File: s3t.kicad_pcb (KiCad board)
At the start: 2 copper layers, 1 part

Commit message: add some lib
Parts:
- removed REF**: S3Core, s3core:S3Core
- added C1, C5: 10uF, Capacitors_SMD:C_0805, F.Cu at (148.5, 105.0)
- added C10, C14, C17, C19, C9: 0.1uF, Capacitors_SMD:C_0603, F.Cu at (148.5, 105.0)
- added C18: 4.7uF, Capacitors_SMD:C_0603, F.Cu at (148.5, 105.0)
- added C2, C4: 100nF, Capacitors_SMD:C_0603, F.Cu at (148.5, 105.0)
- added C3: C, Resistors_SMD:R_0603, F.Cu at (148.5, 105.0)
- added C6: 47uF, Capacitors_THT:CP_Radial_D8.0mm_P2.50mm, F.Cu at (148.5, 105.0)
- added C7, C8: 7pF, Capacitors_SMD:C_0603, F.Cu at (148.5, 105.0)
- added D1, D2: BAV99LT1G, TO_SOT_Packages_SMD:SOT-23, F.Cu at (148.5, 105.0)
- added D3, D4, D5: LED, LEDs:LED_0805, F.Cu at (148.5, 105.0)
- added D6: D, Diodes_SMD:D_1206, F.Cu at (148.5, 105.0)
- added J3: USB_OTG, Connectors:USB_Mini-B, F.Cu at (148.5, 105.0)
- added L1: 1uH, Inductors_SMD:L_7.3x7.3_H3.5, F.Cu at (148.5, 105.0)
- added L2: 1uH, Inductors_SMD:L_1812, F.Cu at (148.5, 105.0)
- added R1: 100K, Resistors_SMD:R_0603, F.Cu at (148.5, 105.0)
- added R10, R6, R8, R9: R, Resistors_SMD:R_0603, F.Cu at (148.5, 105.0)
- added R12, R14: 1K, Resistors_SMD:R_0603, F.Cu at (148.5, 105.0)
- added R17: 10K, Resistors_SMD:R_0603, F.Cu at (148.5, 105.0)
- added R18: 10K2, Capacitors_SMD:C_0603, F.Cu at (148.5, 105.0)
- added R2: 6.8K, Resistors_SMD:R_0603, F.Cu at (148.5, 105.0)
- added R3, R4: 8.2K, Resistors_SMD:R_0603, F.Cu at (148.5, 105.0)
- added R5, R7: 12K, Resistors_SMD:R_0603, F.Cu at (148.5, 105.0)
- added U1: AMS1117-3.3, TO_SOT_Packages_SMD:SOT-223, F.Cu at (148.5, 105.0)
- added U2: TF_CARD, tfcard:tfcard, F.Cu at (148.5, 105.0)
- added U3: s3core, s3core:S3Core, F.Cu at (148.5, 105.0)
- added U4: SX1308, TO_SOT_Packages_SMD:SOT-23-6, F.Cu at (148.5, 105.0)
- added U5: PT4103, TO_SOT_Packages_SMD:SOT-23-6, F.Cu at (148.5, 105.0)
- added U6: THERMAL, fpc36:Hirose_FH12-36S-0.5SH_1x36-1MP_P0.50mm_Horizontal, F.Cu at (148.5, 105.0)
- added U7: LCD_A050FW01, fpc40:Hirose_FH12-40S-0.5SH_1x40-1MP_P0.50mm_Horizontal, F.Cu at (148.5, 105.0)

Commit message: update pcb lib
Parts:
- added C15: C, Capacitors_SMD:C_0603, F.Cu at (86.0, 79.4)
- added J1: DEBUG_UART0, Connectors_JST:JST_EH_B04B-EH-A_04x2.50mm_Straight, F.Cu at (133.2, 67.6)
- added R15: R, Resistors_SMD:R_0805, F.Cu at (50.5, 61.9)
- added R16: R, Resistors_SMD:R_0805, F.Cu at (67.6, 56.8)
- added SW1: SW_DIP_x01, tfcard:button, F.Cu at (87.3, 100.7)
- added SW2: SW_DIP_x01, tfcard:button, F.Cu at (64.0, 136.7)
- added SW3: SW_DIP_x01, tfcard:button, F.Cu at (91.8, 51.6)
- added SW4: SW_DIP_x01, tfcard:button, F.Cu at (68.3, 65.9)
- added SW5: SW_DIP_x01, tfcard:button, F.Cu at (39.1, 81.2)
- added SW6: SW_DIP_x01, tfcard:button, F.Cu at (70.3, 45.2)
- C3: value C -> 0.1uF
- L1: footprint Inductors_SMD:L_7.3x7.3_H3.5 -> Inductors_SMD:L_1812
- R6: value R -> 10K
- moved L1 116.4 mm to (46.0, 49.8)
- moved U1 58.8 mm to (203.5, 84.3)
- moved U3 46.2 mm to (192.3, 119.6)
- moved U2 36.1 mm to (144.9, 140.9)
- moved C6 25.5 mm to (126.3, 92.4)
- moved C1 25.4 mm to (172.6, 97.0)
- moved U7 23.5 mm to (162.8, 86.4)
- moved U6 19.3 mm to (129.6, 109.1)
- moved C2 17.9 mm to (163.4, 114.8)
- moved L2 16.8 mm to (165.1, 107.6)
- moved J3 14.0 mm to (139.4, 94.4)
- moved D1 13.4 mm to (161.1, 100.4)
- moved C4 11.5 mm to (150.3, 116.4)
- moved D2 9.74 mm to (156.4, 110.6)
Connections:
- U2 pad 12: GND -> (no net)

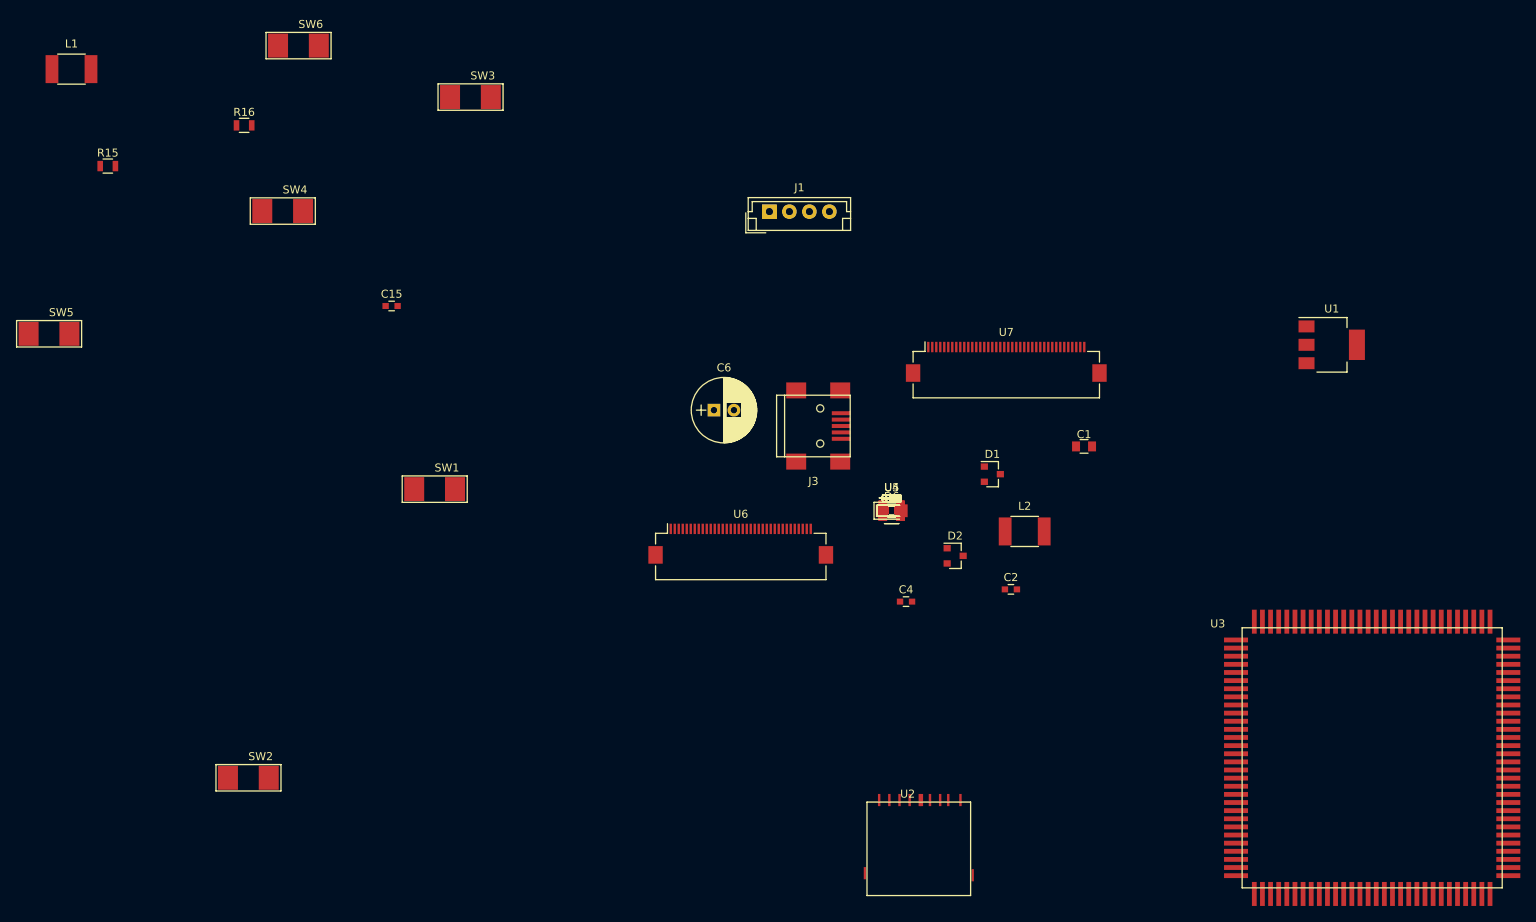
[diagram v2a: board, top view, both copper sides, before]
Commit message: update pcb route
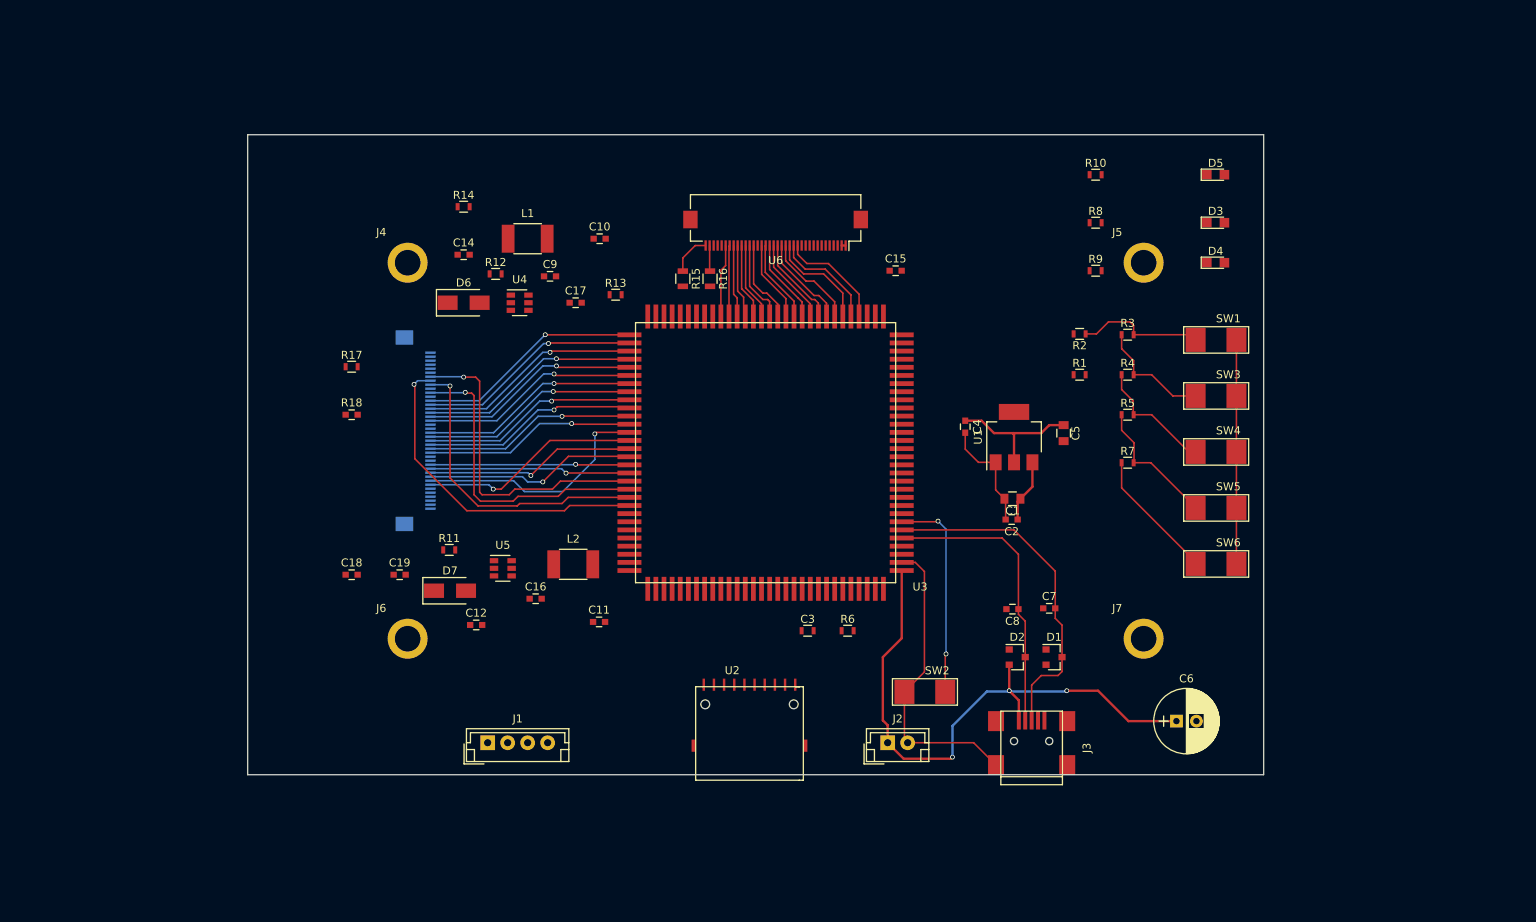
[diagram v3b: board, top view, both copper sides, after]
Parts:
- added C11: 0.1uF, Capacitors_SMD:C_0603, F.Cu at (111.9, 118.9)
- added C12: 0.1uF, Capacitors_SMD:C_0603, F.Cu at (96.6, 119.3)
- added C16: 0.1uF, Capacitors_SMD:C_0603, F.Cu at (104.0, 116.0)
- added D7: D, Diodes_SMD:D_SMA, F.Cu at (93.3, 115.0)
- added J2: Conn_01x02, Connectors_JST:JST_EH_B02B-EH-A_02x2.50mm_Straight, F.Cu at (148.0, 134.0)
- added J4: HOLE, hole:hole, F.Cu at (88.0, 74.0)
- added J5: HOLE, hole:hole, F.Cu at (180.0, 74.0)
- added J6: HOLE, hole:hole, F.Cu at (88.0, 121.0)
- added J7: HOLE, hole:hole, F.Cu at (180.0, 121.0)
- added R11: 5R1, Resistors_SMD:R_0603, F.Cu at (93.2, 109.9)
- added R13: R, Resistors_SMD:R_0603, F.Cu at (114.0, 78.0)
- D6: footprint Diodes_SMD:D_1206 -> Diodes_SMD:D_SMA
- U7: moved to B.Cu
- moved SW5 147.5 mm to (185.0, 103.0)
- moved SW6 131.7 mm to (185.0, 110.0)
- moved SW4 120.5 mm to (185.0, 96.0)
- moved SW3 100.4 mm to (185.0, 89.0)
- moved SW1 99.4 mm to (185.0, 82.0)
- moved SW2 85.2 mm to (148.6, 126.0)
- moved J1 75.2 mm to (98.0, 134.0)
- moved U7 74.3 mm to (89.0, 95.0), turned to 90 degrees
- moved R15 73.2 mm to (122.4, 76.0), turned to 270 degrees
- moved R17 69.9 mm to (81.0, 87.0)
- moved C6 69.7 mm to (184.1, 131.3)
- moved R18 68.6 mm to (81.0, 93.0)
- moved C18 68.0 mm to (81.0, 113.0)
- moved R14 65.6 mm to (95.0, 67.0)
- moved C15 63.2 mm to (149.0, 75.0)
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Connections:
- C7 pad 2: +5V -> /USBDP
- C8 pad 1: +5V -> /USBDN
- D1 pad 3: +5V -> /USBDP
- D2 pad 3: +5V -> /USBDN
- J3 pad 2: +5V -> /USBDN
- J3 pad 3: +5V -> /USBDP
- U3 pad 5: +5V -> /USBDN
- U3 pad 6: +5V -> /USBDP
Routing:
- net +5V: track 0.00 -> 82.7 mm, vias 0 -> 3
- net GND: track 0.00 -> 80.3 mm
- net /USBDP: track 0.00 -> 43.1 mm
- net /LCD_VSYNC: track 0.00 -> 41.4 mm, vias 0 -> 1
- net /LCD_DE: track 0.00 -> 39.8 mm, vias 0 -> 1
- net /LCD_CLK: track 0.00 -> 38.4 mm, vias 0 -> 1
- net /LCD_HSYNC: track 0.00 -> 38.3 mm, vias 0 -> 1
- net /USBDN: track 0.00 -> 36.5 mm
- net /LCD_D19: track 0.00 -> 30.4 mm, vias 0 -> 1
- net /LCD_D7: track 0.00 -> 28.3 mm, vias 0 -> 1
- net /LCD_D6: track 0.00 -> 28.1 mm, vias 0 -> 1
- net /LCD_D5: track 0.00 -> 27.9 mm, vias 0 -> 1
- net /LCD_D4: track 0.00 -> 27.7 mm, vias 0 -> 1
- net /LCD_D18: track 0.00 -> 27.6 mm, vias 0 -> 1
- net /LCD_D3: track 0.00 -> 27.6 mm, vias 0 -> 1
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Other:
- board outline added: 127 x 80 mm
- net class +3V3 added: clearance 0.15, trace_width 0.3, via_dia 0.6, via_drill 0.4
- net class +5V added: clearance 0.15, trace_width 0.3, via_dia 0.6, via_drill 0.4
- net class 9.5V added: clearance 0.15, trace_width 0.3, via_dia 0.6, via_drill 0.4
- net class Default: clearance 0.2 -> 0.15; trace_width 0.25 -> 0.2
- net class GND added: clearance 0.15, trace_width 0.2, via_dia 0.6, via_drill 0.4
- rule trace_clearance: 0.2 -> 0.15

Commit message: update pcb
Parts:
- C3, R17, R18, R6: moved to B.Cu
- moved J1 88.8 mm to (157.1, 67.7)
- moved R13 44.6 mm to (99.0, 120.0)
- moved C18 17.9 mm to (86.1, 130.2)
- moved L2 17.8 mm to (106.8, 129.4)
- moved C11 16.4 mm to (111.9, 135.3)
- moved D7 14.9 mm to (95.4, 129.8)
- moved R6 14.2 mm to (134.8, 131.6), turned to 180 degrees
- moved C3 14.0 mm to (130.0, 131.5)
- moved U5 11.1 mm to (105.1, 122.0)
- moved R12 7.44 mm to (99.8, 82.8)
- moved C15 5.83 mm to (143.2, 74.4), turned to 180 degrees
- moved C12 5.56 mm to (98.2, 124.6)
- moved R11 5.19 mm to (96.1, 114.2)
- moved C10 3.35 mm to (108.8, 72.0)
- turned D3 to 180 degrees
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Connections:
- U3 pad 32: /TCLK -> /TPCLK
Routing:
- net GND: track 80.3 -> 415.1 mm, vias 0 -> 11
- net +5V: track 82.7 -> 222.2 mm, vias 3 -> 7
- net /9.5V: track 0.50 -> 111.3 mm, vias 0 -> 4
- net +3V3: track 17.2 -> 98.5 mm, vias 0 -> 5
- net /LED3: track 0.00 -> 79.4 mm, vias 0 -> 2
- net /LED2: track 0.00 -> 75.0 mm, vias 0 -> 2
- net /TEN: track 0.00 -> 47.4 mm, vias 0 -> 2
- net /LRADC0: track 0.00 -> 39.8 mm
- net /UART1_TX: track 0.00 -> 39.2 mm, vias 0 -> 2
- net /UART1_RX: track 0.00 -> 37.1 mm, vias 0 -> 2
- net /SD_DAT2: track 0.00 -> 32.8 mm, vias 0 -> 2
- net /SD_DAT3: track 0.00 -> 30.7 mm, vias 0 -> 2
- net /TPCLK: track 0.00 -> 30.3 mm
- net /SD_CMD: track 0.00 -> 26.9 mm
- net /RXD0: track 0.00 -> 26.3 mm
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
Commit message: finish pcb route
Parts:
- moved L2 26.9 mm to (80.0, 127.5), turned to 90 degrees
- moved C18 26.2 mm to (80.6, 104.6)
- moved C11 25.1 mm to (87.9, 127.8), turned to 90 degrees
- moved R11 16.9 mm to (98.2, 131.0)
- moved D7 14.5 mm to (102.3, 117.0), turned to 180 degrees
- moved R13 12.5 mm to (105.0, 131.0), turned to 180 degrees
- moved C6 10.9 mm to (195.0, 132.0)
- moved D4 8.06 mm to (197.0, 75.0)
- moved U5 8.03 mm to (97.5, 124.6)
- moved D3 8.00 mm to (197.0, 69.0)
- moved D5 8.00 mm to (197.0, 63.0)
- moved C19 7.77 mm to (80.4, 108.9)
- moved SW1 7.00 mm to (192.0, 82.0)
- moved SW3 7.00 mm to (192.0, 89.0)
- moved SW4 7.00 mm to (192.0, 96.0)
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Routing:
- net GND: track 415.1 -> 774.0 mm, vias 11 -> 22
- net +3V3: track 98.5 -> 252.1 mm, vias 5 -> 8
- net +5V: track 222.2 -> 329.1 mm, vias 7 -> 8
- net /LCD_EN: track 0.00 -> 75.0 mm, vias 0 -> 2
- net /LEDK: track 0.00 -> 44.1 mm, vias 0 -> 1
- net /LEDA: track 0.00 -> 38.9 mm, vias 0 -> 1
- net Net-(D7-Pad2): track 0.00 -> 27.4 mm
- net /LED2: track 75.0 -> 83.6 mm
- net Net-(D4-Pad2): track 15.7 -> 24.1 mm
- net Net-(D5-Pad2): track 13.2 -> 21.2 mm
- net Net-(D3-Pad2): track 13.2 -> 21.2 mm
- net /LED3: track 79.4 -> 87.2 mm
- net Net-(R4-Pad1): track 15.3 -> 22.3 mm
- net Net-(R3-Pad1): track 14.5 -> 21.5 mm
- net Net-(R2-Pad1): track 16.0 -> 23.0 mm
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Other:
- board size 127 x 80 mm -> 134 x 80 mm

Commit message: finish all pcb and send to factory
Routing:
- added copper zone on B.Cu, net GND
- added copper zone on F.Cu, net GND
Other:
- outline, holes or cut-outs redrawn
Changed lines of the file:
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@@
   (general
     (links 203)
-    (no_connects 3)
-    (area 67.924999 34.8 202.075001 139.675001)
+    (no_connects 0)
+    (area 50.150002 34.8 202.075001 152.7)
     (thickness 1.6)
-    (drawings 10)
+    (drawings 18)
     (tracks 1003)
     (zones 0)
@@
     (trace_clearance 0.15)
     (zone_clearance 0.508)
-    (zone_45_only no)
+    (zone_45_only yes)
     (trace_min 0.2)
     (segment_width 0.2)
@@
     (pad "" np_thru_hole circle (at 0.2 2.2 90) (size 0.9 0.9) (drill 0.9) (layers *.Cu *.Mask))
   )
+  (gr_line (start 124.6 89.6) (end 124.8 89.6) (angle 90) (layer Edge.Cuts) (width 0.15))
+  (gr_line (start 124.6 105.9) (end 124.6 89.6) (angle 90) (layer Edge.Cuts) (width 0.15))
+  (gr_line (start 140.9 105.9) (end 124.6 105.9) (angle 90) (layer Edge.Cuts) (width 0.15))
+  (gr_line (start 140.9 89.6) (end 140.9 105.9) (angle 90) (layer Edge.Cuts) (width 0.15))
+  (gr_line (start 124.6 89.6) (end 140.9 89.6) (angle 90) (layer Edge.Cuts) (width 0.15))
+  (gr_line (start 140.9 105.9) (end 140.9 89.6) (angle 90) (layer Edge.Cuts) (width 0.15))
+  (gr_line (start 124.6 105.9) (end 140.9 105.9) (angle 90) (layer Edge.Cuts) (width 0.15))
+  (gr_line (start 124.6 89.6) (end 124.6 105.9) (angle 90) (layer Edge.Cuts) (width 0.15))
   (dimension 134 (width 0.3) (layer Dwgs.User)
     (gr_text "134.000 mm" (at 135 151.349999) (layer Dwgs.User)
@@
   (segment (start 189.1 131.3) (end 190.9 131.3) (width 0.3) (layer F.Cu) (net 1))
   (segment (start 184 131.3) (end 189.1 131.3) (width 0.3) (layer F.Cu) (net 1))
-  (segment (start 191.6 132) (end 195 132) (width 0.3) (layer F.Cu) (net 1) (status 800000))
+  (segment (start 191.6 132) (end 195 132) (width 0.3) (layer F.Cu) (net 1))
   (segment (start 190.9 131.3) (end 191.6 132) (width 0.3) (layer F.Cu) (net 1))
   (segment (start 171.1 118.7) (end 176.9 118.7) (width 0.3) (layer B.Cu) (net 1))
@@
   (segment (start 164.25 103.85) (end 166.1 102) (width 0.3) (layer F.Cu) (net 1))
   (segment (start 166.1 102) (end 166.1 98.95) (width 0.3) (layer F.Cu) (net 1))
-  (segment (start 197.5 132) (end 197.5 128.5) (width 0.2) (layer F.Cu) (net 2) (status 400000))
+  (segment (start 197.5 132) (end 197.5 128.5) (width 0.2) (layer F.Cu) (net 2))
   (segment (start 197.5 128.5) (end 194.6 125.6) (width 0.2) (layer F.Cu) (net 2))
   (segment (start 99.1 77.9) (end 90.5 77.9) (width 0.2) (layer B.Cu) (net 2))
@@
   (segment (start 165.2 118.8) (end 164.35 117.95) (width 0.2) (layer F.Cu) (net 142))
   (segment (start 165.2 131.2) (end 165.2 123.3) (width 0.2) (layer F.Cu) (net 142))
+  (zone (net 0) (net_name "") (layer F.Cu) (hatch edge 0.508)
+    (connect_pads (clearance 0.508))
+    (min_thickness 0.254)
+    (keepout (tracks not_allowed) (vias allowed) (copperpour not_allowed))
+    (fill (arc_segments 16) (thermal_gap 0.508) (thermal_bridge_width 0.508))
+    (polygon
+      (pts
+        (xy 140.9 105.9) (xy 124.6 105.9) (xy 124.6 89.6) (xy 140.9 89.6)
+      )
+    )
+  )
+  (zone (net 2) (net_name GND) (layer F.Cu) (hatch edge 0.508)
+    (connect_pads (clearance 0.508))
+    (min_thickness 0.254)
+    (fill yes (arc_segments 16) (thermal_gap 0.508) (thermal_bridge_width 0.508))
+    (polygon
+      (pts
+        (xy 202 138) (xy 68 138) (xy 68 58) (xy 202 58)
+      )
+    )
+  )
+  (zone (net 0) (net_name "") (layer B.Cu) (hatch edge 0.508)
+    (connect_pads (clearance 0.508))
+    (min_thickness 0.254)
+    (keepout (tracks not_allowed) (vias allowed) (copperpour not_allowed))
+    (fill (arc_segments 16) (thermal_gap 0.508) (thermal_bridge_width 0.508))
+    (polygon
+      (pts
+        (xy 140.9 105.9) (xy 124.6 105.9) (xy 124.6 89.6) (xy 140.9 89.6)
+      )
+    )
+  )
+  (zone (net 2) (net_name GND) (layer B.Cu) (hatch edge 0.508)
+    (connect_pads (clearance 0.508))
+    (min_thickness 0.254)
+    (fill yes (arc_segments 16) (thermal_gap 0.508) (thermal_bridge_width 0.508))
+    (polygon
+      (pts
+        (xy 202 138) (xy 68 138) (xy 68 58) (xy 202 58)
+      )
+    )
+  )
 )
